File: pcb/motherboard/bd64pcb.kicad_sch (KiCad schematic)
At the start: 224 parts, among them J1 Conn_01x04, J2 Conn_01x04, J3 Conn_01x04, SW1 SW_Push, U1 ATmega32U4-MU, U2 IS31FL3733-QF, Y1 16MHz

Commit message: organizing sch components
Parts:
- added J? (x3): Conn_01x04, Connector_JST:JST_SUR_SM04B-SURS-TF_1x04-1MP_P0.80mm_Horizontal, symbol Connector_Generic:Conn_01x04
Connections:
- net +5V: now also J?.1 (Pin_1), J?.2 (Pin_2), J?.2 (Pin_2)
- net D+: now also J?.3 (Pin_3)
- net D-: now also J?.2 (Pin_2)
- net GND: now also J?.1 (Pin_1), J?.1 (Pin_1), J?.4 (Pin_4), J?.MP, J?.MP, J?.MP
- net SCL: now also J?.4 (Pin_4), J?.4 (Pin_4)
- net SDA: now also J?.3 (Pin_3), J?.3 (Pin_3)
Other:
- note added: "Alt"
- note added: "Daughterboard connections"
- note added: "Decoupling net"
- note added: "MCU"
- note added: "OG"
- note added: "Per-key RGB matrix"
- note added: "RGB driver"
- note added: "Switch matrix"
- note added: "front touchpad"
- note added: "left touchpad"
- note added: "usbc"
- moved on the sheet: C1, C10, C11, C12, C13, C14, C15, C16, C2, C3, C4, C5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

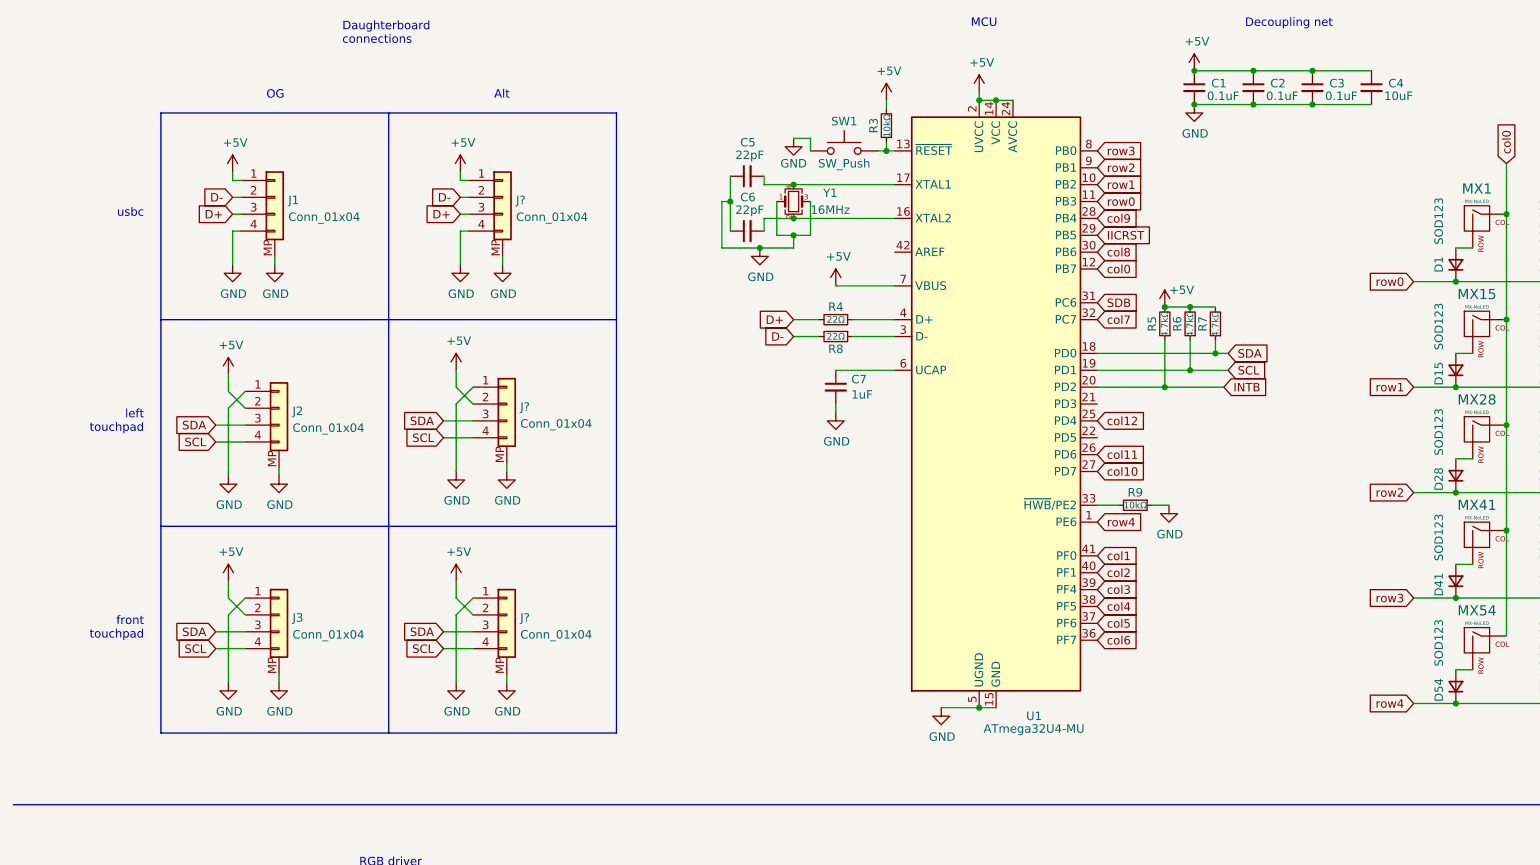
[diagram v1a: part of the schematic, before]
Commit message: removing alt connectors
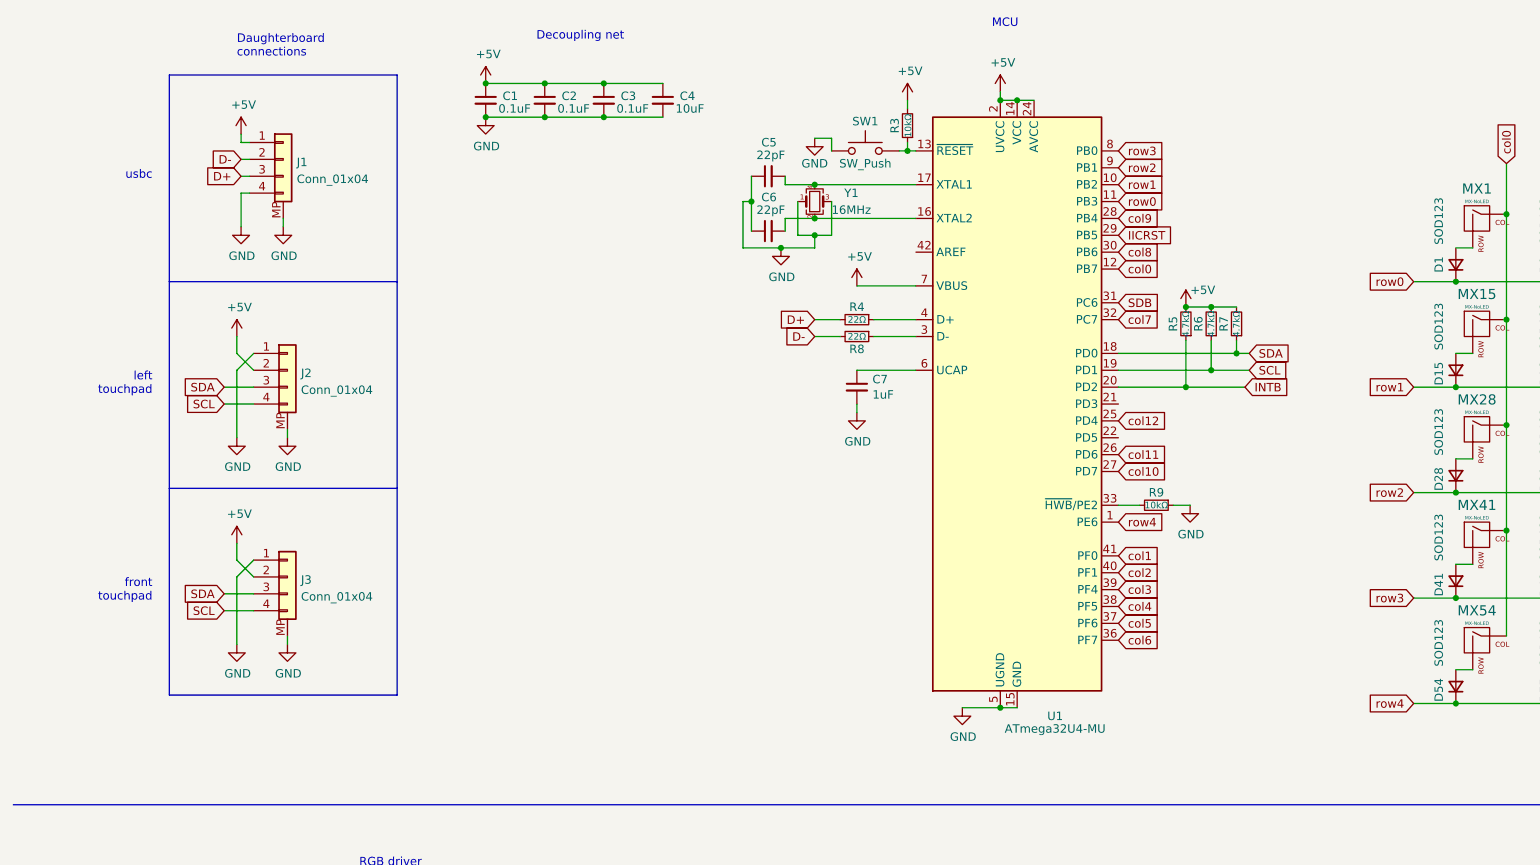
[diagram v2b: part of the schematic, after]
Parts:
- removed J? (x3): Conn_01x04, Connector_JST:JST_SUR_SM04B-SURS-TF_1x04-1MP_P0.80mm_Horizontal, symbol Connector_Generic:Conn_01x04
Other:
- note removed: "Alt"
- note removed: "OG"
- moved on the sheet: C1, C2, C3, C4, C5, C6, C7, J1, J2, J3, R3, R4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

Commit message: usbc connector from SUR to SH
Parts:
- J1: footprint Connector_JST:JST_SUR_SM04B-SURS-TF_1x04-1MP_P0.80mm_Horizontal -> Connector_JST:JST_SH_SM04B-SRSS-TB_1x04-1MP_P1.00mm_Horizontal
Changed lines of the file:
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@@
       (effects (font (size 1.27 1.27)) (justify left))
     )
-    (property "Footprint" "Connector_JST:JST_SUR_SM04B-SURS-TF_1x04-1MP_P0.80mm_Horizontal" (id 2) (at 52.705 42.545 0)
+    (property "Footprint" "Connector_JST:JST_SH_SM04B-SRSS-TB_1x04-1MP_P1.00mm_Horizontal" (id 2) (at 52.705 42.545 0)
       (effects (font (size 1.27 1.27)) hide)
     )
@@
     )
     (path "/249794d8-9f77-48d5-82c2-e90268fabe6e"
-      (reference "J1") (unit 1) (value "Conn_01x04") (footprint "Connector_JST:JST_SUR_SM04B-SURS-TF_1x04-1MP_P0.80mm_Horizontal")
+      (reference "J1") (unit 1) (value "Conn_01x04") (footprint "Connector_JST:JST_SH_SM04B-SRSS-TB_1x04-1MP_P1.00mm_Horizontal")
     )
     (path "/bfedb103-5d71-44da-9b77-ab5c7fa95163"

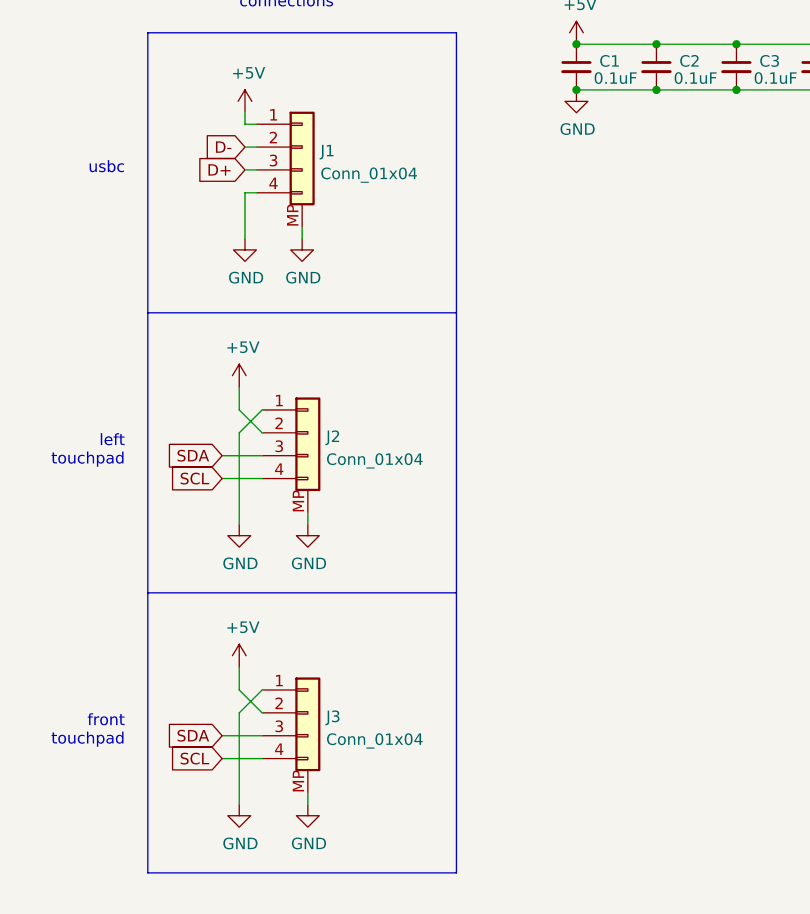
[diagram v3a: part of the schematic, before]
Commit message: update connector values
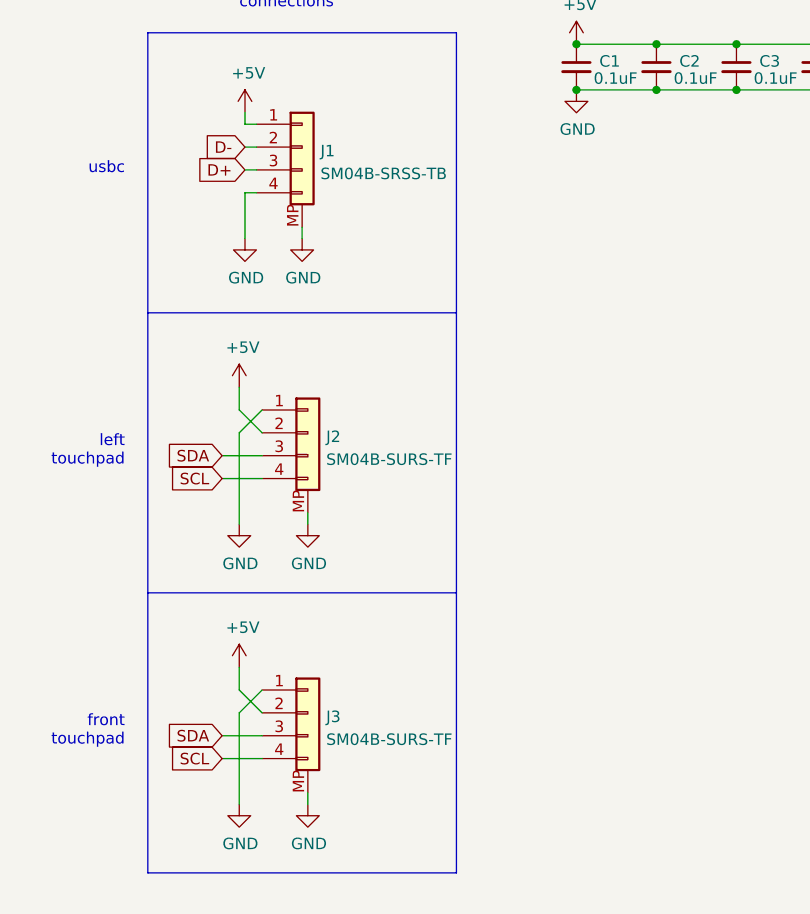
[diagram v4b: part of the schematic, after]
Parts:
- J1: value Conn_01x04 -> SM04B-SRSS-TB
- J2, J3: value Conn_01x04 -> SM04B-SURS-TF
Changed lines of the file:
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@@
       (effects (font (size 1.27 1.27)) (justify left))
     )
-    (property "Value" "Conn_01x04" (id 1) (at 54.737 45.5172 0)
+    (property "Value" "SM04B-SRSS-TB" (id 1) (at 54.737 45.5172 0)
       (effects (font (size 1.27 1.27)) (justify left))
     )
@@
       (effects (font (size 1.27 1.27)) (justify left))
     )
-    (property "Value" "Conn_01x04" (id 1) (at 55.372 108.3822 0)
+    (property "Value" "SM04B-SURS-TF" (id 1) (at 55.372 108.3822 0)
       (effects (font (size 1.27 1.27)) (justify left))
     )
@@
       (effects (font (size 1.27 1.27)) (justify left))
     )
-    (property "Value" "Conn_01x04" (id 1) (at 55.372 77.2672 0)
+    (property "Value" "SM04B-SURS-TF" (id 1) (at 55.372 77.2672 0)
       (effects (font (size 1.27 1.27)) (justify left))
     )
@@
     )
     (path "/249794d8-9f77-48d5-82c2-e90268fabe6e"
-      (reference "J1") (unit 1) (value "Conn_01x04") (footprint "Connector_JST:JST_SH_SM04B-SRSS-TB_1x04-1MP_P1.00mm_Horizontal")
+      (reference "J1") (unit 1) (value "SM04B-SRSS-TB") (footprint "Connector_JST:JST_SH_SM04B-SRSS-TB_1x04-1MP_P1.00mm_Horizontal")
     )
     (path "/bfedb103-5d71-44da-9b77-ab5c7fa95163"
-      (reference "J2") (unit 1) (value "Conn_01x04") (footprint "Connector_JST:JST_SUR_SM04B-SURS-TF_1x04-1MP_P0.80mm_Horizontal")
+      (reference "J2") (unit 1) (value "SM04B-SURS-TF") (footprint "Connector_JST:JST_SUR_SM04B-SURS-TF_1x04-1MP_P0.80mm_Horizontal")
     )
     (path "/986a64bc-99d8-42ad-8dae-e7121e943202"
-      (reference "J3") (unit 1) (value "Conn_01x04") (footprint "Connector_JST:JST_SUR_SM04B-SURS-TF_1x04-1MP_P0.80mm_Horizontal")
+      (reference "J3") (unit 1) (value "SM04B-SURS-TF") (footprint "Connector_JST:JST_SUR_SM04B-SURS-TF_1x04-1MP_P0.80mm_Horizontal")
     )
     (path "/00000000-0000-0000-0000-0000635db64f"

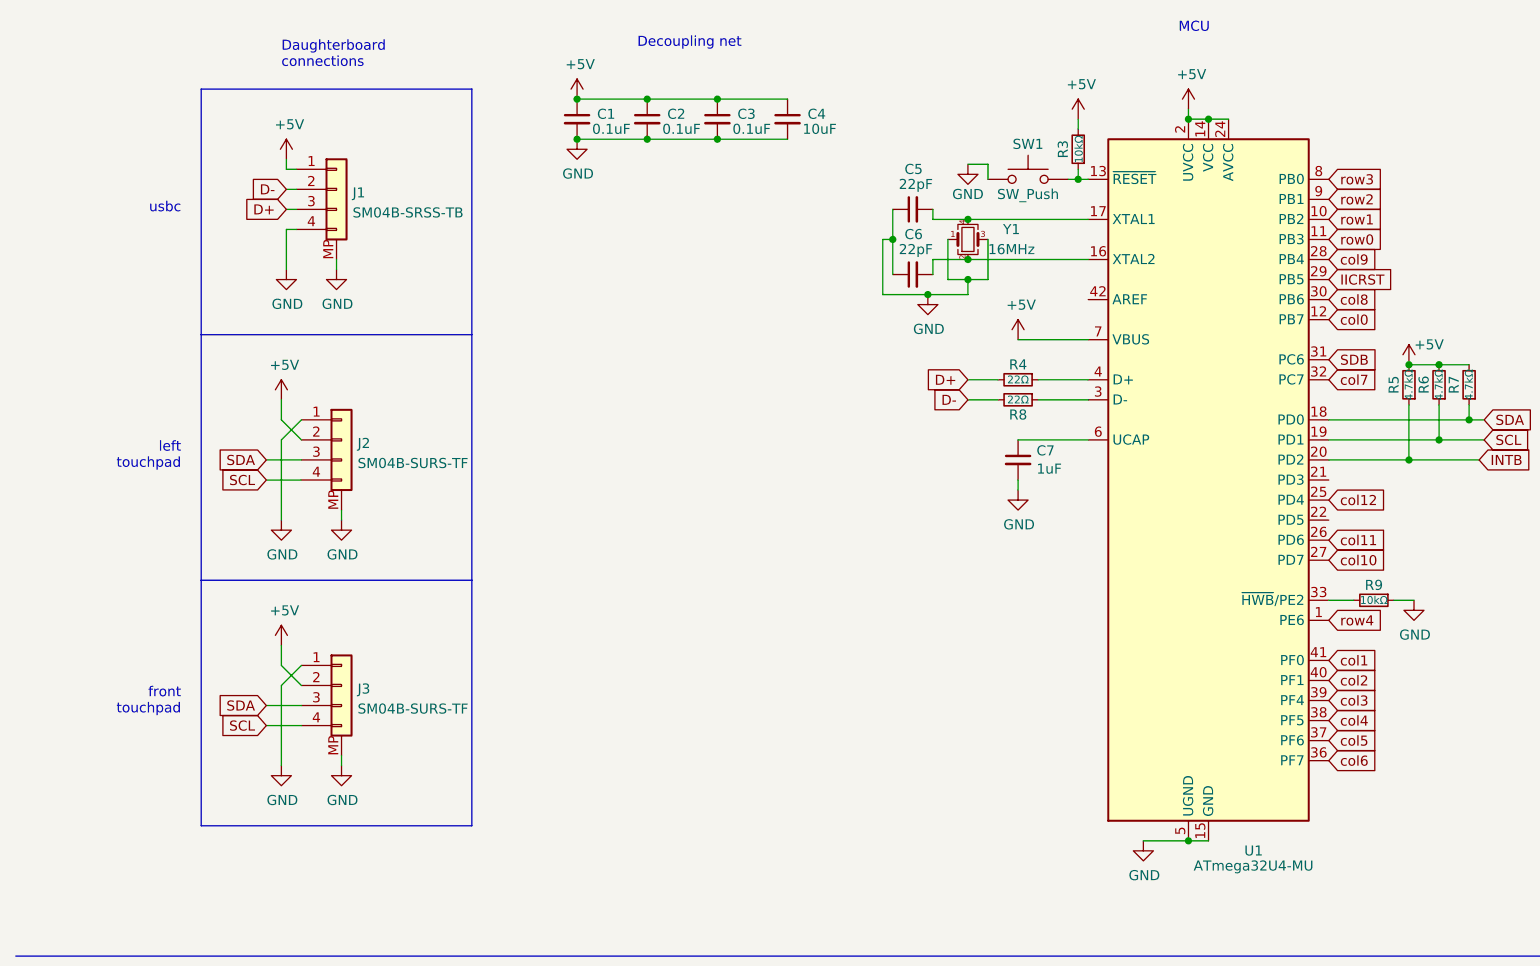
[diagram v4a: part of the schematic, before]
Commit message: 5pin touchpad connector sch
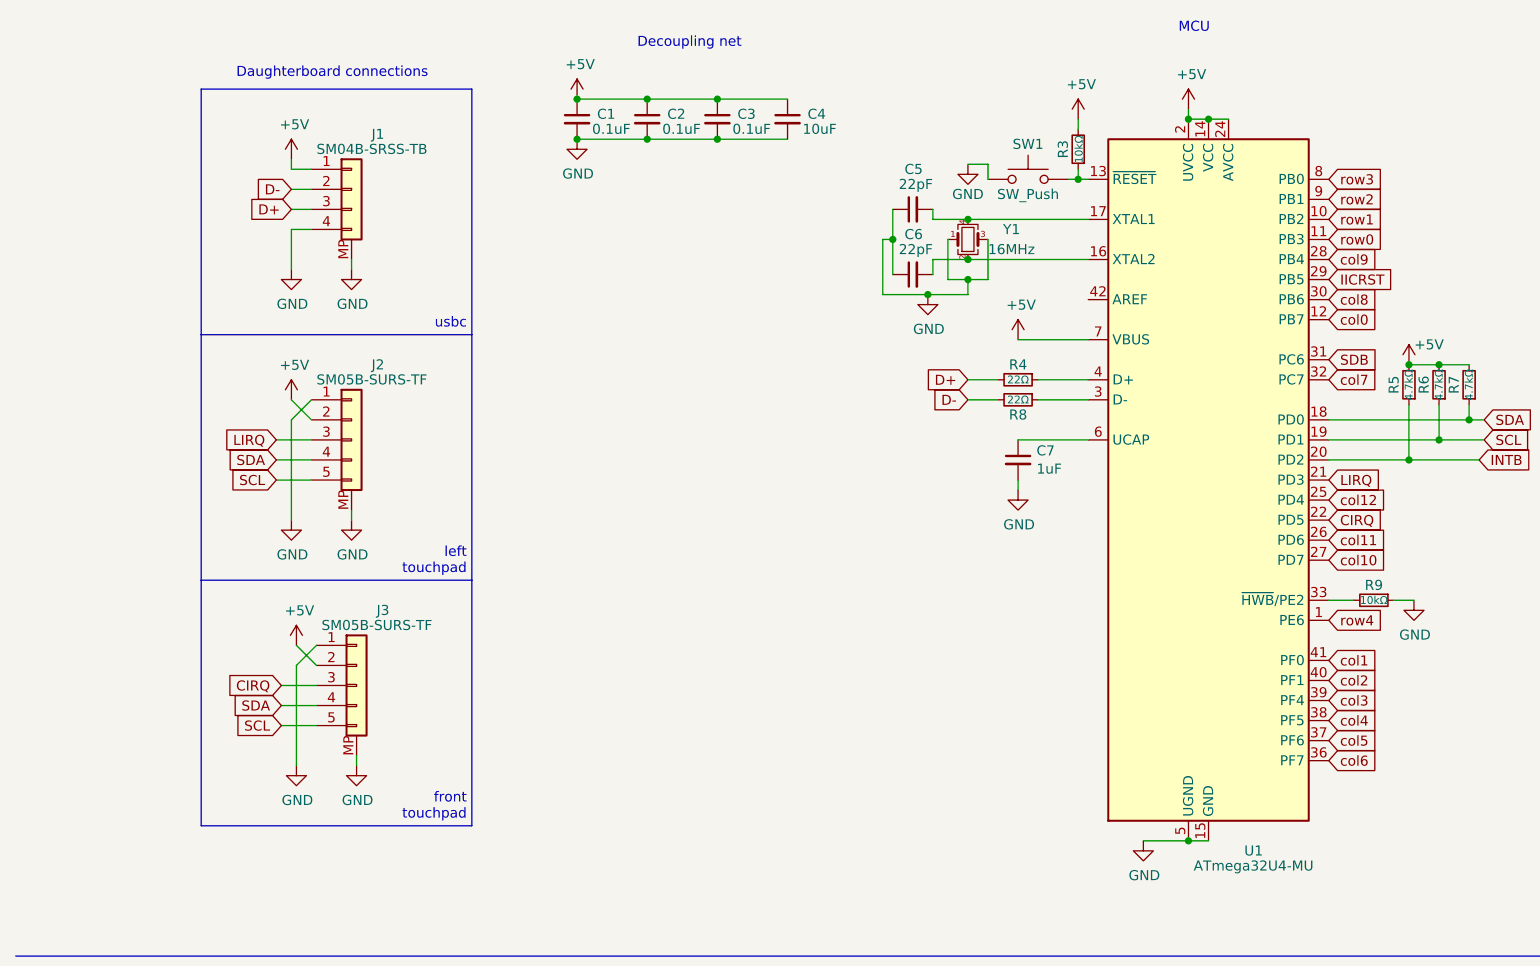
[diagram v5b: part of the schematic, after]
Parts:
- J2, J3: value SM04B-SURS-TF -> SM05B-SURS-TF; symbol Connector_Generic:Conn_01x04 -> Connector_Generic:Conn_01x05
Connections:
- net SCL: now also J2.5 (Pin_5), J3.5 (Pin_5); no longer J2.4 (Pin_4), J3.4 (Pin_4)
- net SDA: now also J2.4 (Pin_4), J3.4 (Pin_4); no longer J2.3 (Pin_3), J3.3 (Pin_3)
- net LIRQ: now reaches U1.21 (PD3)
- net LIRQ: now also J2.3 (Pin_3)
- net CIRQ: now reaches U1.22 (PD5)
- net CIRQ: now also J3.3 (Pin_3)
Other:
- moved on the sheet: J1

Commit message: sm05b footprints and 3d models
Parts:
- J2, J3: footprint Connector_JST:JST_SUR_SM04B-SURS-TF_1x04-1MP_P0.80mm_Horizontal -> Connector_JST:JST_SUR_SM05B-SURS-TF_1x05-1MP_P0.80mm_Horizontal
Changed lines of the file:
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@@
       (effects (font (size 1.27 1.27)) (justify left))
     )
-    (property "Footprint" "Connector_JST:JST_SUR_SM04B-SURS-TF_1x04-1MP_P0.80mm_Horizontal" (id 2) (at 55.245 105.41 0)
+    (property "Footprint" "Connector_JST:JST_SUR_SM05B-SURS-TF_1x05-1MP_P0.80mm_Horizontal" (id 2) (at 55.245 105.41 0)
       (effects (font (size 1.27 1.27)) hide)
     )
@@
       (effects (font (size 1.27 1.27)) (justify left))
     )
-    (property "Footprint" "Connector_JST:JST_SUR_SM04B-SURS-TF_1x04-1MP_P0.80mm_Horizontal" (id 2) (at 54.61 74.295 0)
+    (property "Footprint" "Connector_JST:JST_SUR_SM05B-SURS-TF_1x05-1MP_P0.80mm_Horizontal" (id 2) (at 54.61 74.295 0)
       (effects (font (size 1.27 1.27)) hide)
     )
@@
     )
     (path "/bfedb103-5d71-44da-9b77-ab5c7fa95163"
-      (reference "J2") (unit 1) (value "SM05B-SURS-TF") (footprint "Connector_JST:JST_SUR_SM04B-SURS-TF_1x04-1MP_P0.80mm_Horizontal")
+      (reference "J2") (unit 1) (value "SM05B-SURS-TF") (footprint "Connector_JST:JST_SUR_SM05B-SURS-TF_1x05-1MP_P0.80mm_Horizontal")
     )
     (path "/986a64bc-99d8-42ad-8dae-e7121e943202"
-      (reference "J3") (unit 1) (value "SM05B-SURS-TF") (footprint "Connector_JST:JST_SUR_SM04B-SURS-TF_1x04-1MP_P0.80mm_Horizontal")
+      (reference "J3") (unit 1) (value "SM05B-SURS-TF") (footprint "Connector_JST:JST_SUR_SM05B-SURS-TF_1x05-1MP_P0.80mm_Horizontal")
     )
     (path "/00000000-0000-0000-0000-0000635db64f"
